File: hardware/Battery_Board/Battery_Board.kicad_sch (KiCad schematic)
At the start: 0 parts

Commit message: feat(Hw):Battery_Board_pro_Updated
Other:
- added sheet Batt_Connector (Batt_Connector.kicad_sch)
- added sheet USB (USB.kicad_sch)

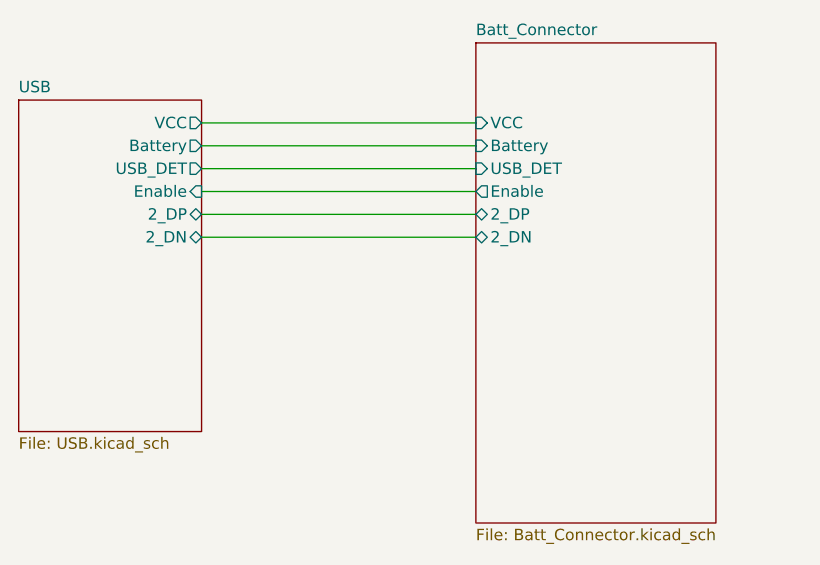
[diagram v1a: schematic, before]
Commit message: feat(Hw):Update_Battery_Sch_And_Sensors_And_PWNCube
pending_Outputs_connectors
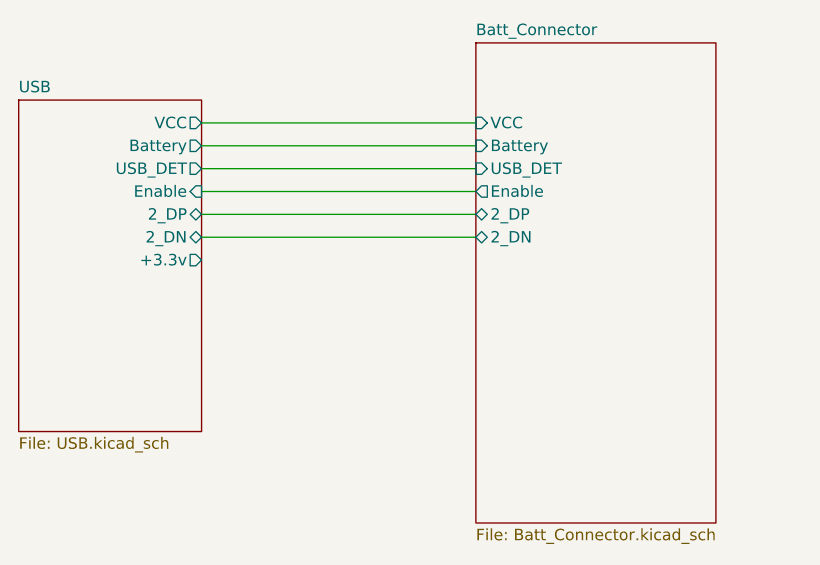
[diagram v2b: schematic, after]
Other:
- sheet USB ports: added +3.3v; removed none
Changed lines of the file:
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@@
+			)
+		)
+		(pin "+3.3v" output
+			(at 134.62 55.88 0)
+			(effects
+				(font
+					(size 1.27 1.27)
+				)
+				(justify right)
 			)
 		)
